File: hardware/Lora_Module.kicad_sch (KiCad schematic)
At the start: 9 parts, among them J2 85201239, U7 RFM95W-868S2

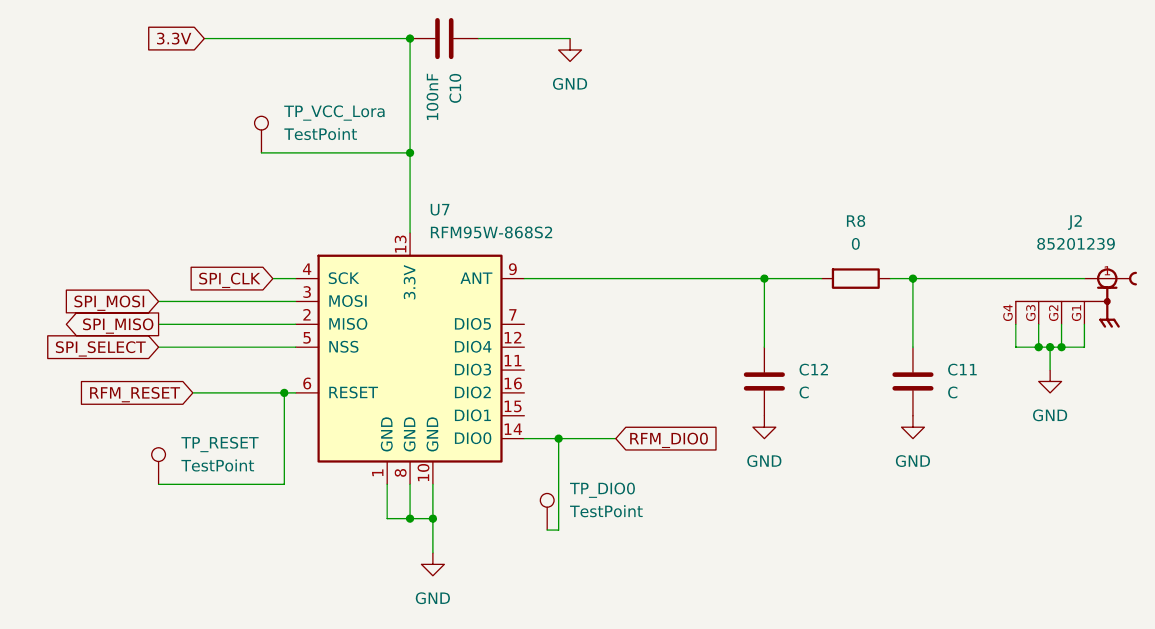
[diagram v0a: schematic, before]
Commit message: Ref composant JLCBPCB LoRa
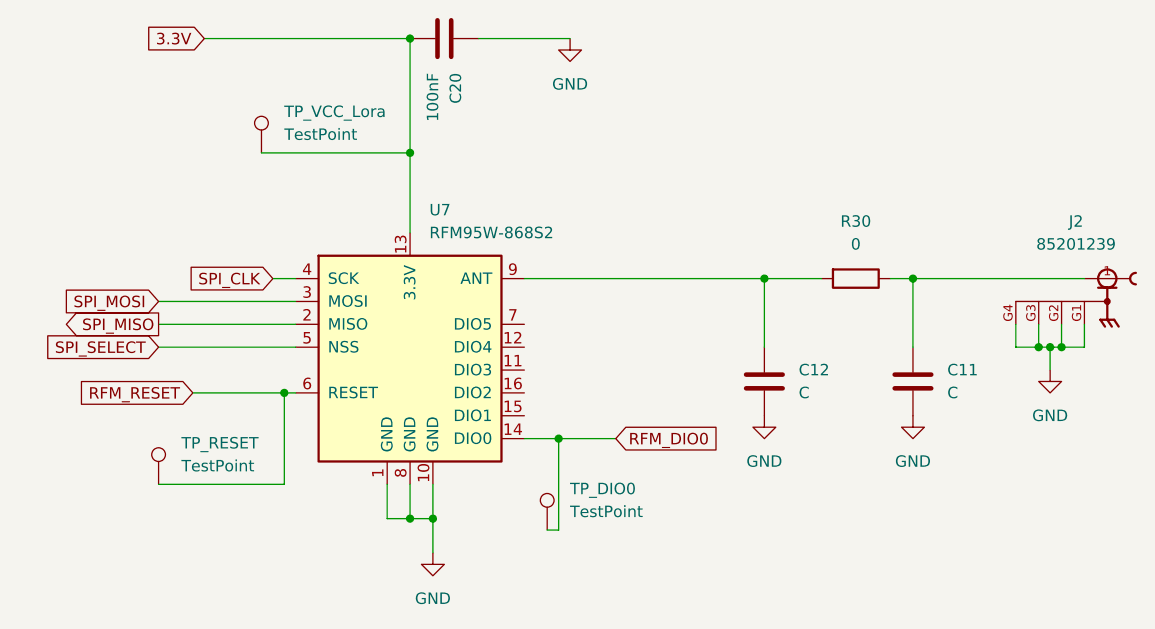
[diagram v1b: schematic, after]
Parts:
- C11, C12: footprint Capacitor_SMD:C_0805_2012Metric_Pad1.18x1.45mm_HandSolder -> Resistor_SMD:R_0805_2012Metric_Pad1.20x1.40mm_HandSolder; JLCPCB Part # (none) -> /; Package (none) -> 0805
- C20: renamed from C10; footprint Capacitor_SMD:C_0201_0603Metric -> Capacitor_SMD:C_0603_1608Metric; JLCPCB Part # (none) -> C1590; Package (none) -> 0603
- J2: JLCPCB Part # (none) -> C7498154; Package None -> Plugin
- R30: renamed from R8; JLCPCB Part # (none) -> /; Package (none) -> 0805
- U7: JLCPCB Part # (none) -> C2844472; Package (none) -> SMD,16x16mm
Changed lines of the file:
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@@
 			)
 		)
-		(property "Description" ""
+		(property "Description" "-45℃~+80℃ 1 14.6mm 4.65mm 50Ω 6GHz Board Side Inner Bore Plugin Coaxial Connectors (RF) ROHS"
 			(at 186.69 64.77 0)
 			(effects
@@
 			)
 		)
-		(property "Package" "None"
+		(property "Package" "Plugin"
 			(at 186.69 64.77 0)
 			(effects
@@
 				)
 				(justify bottom)
+				(hide yes)
+			)
+		)
+		(property "JLCPCB Part #" "C7498154"
+			(at 186.69 64.77 0)
+			(effects
+				(font
+					(size 1.27 1.27)
+				)
 				(hide yes)
 			)
@@
 			)
 		)
-		(property "Footprint" "Capacitor_SMD:C_0805_2012Metric_Pad1.18x1.45mm_HandSolder"
+		(property "Footprint" "Resistor_SMD:R_0805_2012Metric_Pad1.20x1.40mm_HandSolder"
 			(at 149.5552 80.01 0)
 			(effects
@@
 		)
 		(property "Description" "Unpolarized capacitor"
+			(at 148.59 76.2 0)
+			(effects
+				(font
+					(size 1.27 1.27)
+				)
+				(hide yes)
+			)
+		)
+		(property "JLCPCB Part #" "/"
+			(at 148.59 76.2 0)
+			(effects
+				(font
+					(size 1.27 1.27)
+				)
+				(hide yes)
+			)
+		)
+		(property "Package" "0805"
 			(at 148.59 76.2 0)
 			(effects
@@
 		(dnp no)
 		(fields_autoplaced yes)
-		(property "Reference" "R8"
+		(property "Reference" "R30"
 			(at 158.75 58.42 90)
 			(effects
@@
 			)
 		)
+		(property "Package" "0805"
+			(at 158.75 64.77 90)
+			(effects
+				(font
+					(size 1.27 1.27)
+				)
+				(hide yes)
+			)
+		)
+		(property "JLCPCB Part #" "/"
+			(at 158.75 64.77 90)
+			(effects
+				(font
+					(size 1.27 1.27)
+				)
+				(hide yes)
+			)
+		)
 		(pin "1"
 		)
@@
 			(project ""
 				(path "/5b969f6e-a36e-432b-8f00-b2d6a515a877/9db73a32-37a4-4249-8656-c1ba9b3afe01"
-					(reference "R8")
+					(reference "R30")
 					(unit 1)
 				)
@@
 			)
 		)
-		(property "Footprint" "Capacitor_SMD:C_0805_2012Metric_Pad1.18x1.45mm_HandSolder"
+		(property "Footprint" "Resistor_SMD:R_0805_2012Metric_Pad1.20x1.40mm_HandSolder"
 			(at 166.0652 80.01 0)
 			(effects
@@
 		)
 		(property "Description" "Unpolarized capacitor"
+			(at 165.1 76.2 0)
+			(effects
+				(font
+					(size 1.27 1.27)
+				)
+				(hide yes)
+			)
+		)
+		(property "JLCPCB Part #" "/"
+			(at 165.1 76.2 0)
+			(effects
+				(font
+					(size 1.27 1.27)
+				)
+				(hide yes)
+			)
+		)
+		(property "Package" "0805"
 			(at 165.1 76.2 0)
 			(effects
@@
 			)
 		)
+		(property "JLCPCB Part #" "C2844472"
+			(at 109.22 72.39 0)
+			(effects
+				(font
+					(size 1.27 1.27)
+				)
+				(hide yes)
+			)
+		)
+		(property "Package" "SMD,16x16mm"
+			(at 109.22 72.39 0)
+			(effects
+				(font
+					(size 1.27 1.27)
+				)
+				(hide yes)
+			)
+		)
 		(pin "3"
 		)
@@
 		(on_board yes)
 		(dnp no)
-		(property "Reference" "C10"
+		(property "Reference" "C20"
 			(at 114.3001 41.91 0)
 			(effects
@@
 			)
 		)
-		(property "Footprint" "Capacitor_SMD:C_0201_0603Metric"
+		(property "Footprint" "Capacitor_SMD:C_0603_1608Metric"
 			(at 109.22 39.0652 0)
 			(effects
@@
 			)
 		)
-		(property "Description" "Unpolarized capacitor"
+		(property "Description" "100nF 25V X7R ±10% 0603 Multilayer Ceramic Capacitors MLCC - SMD/SMT ROHS"
 			(at 113.03 38.1 0)
 			(effects
@@
 			)
 		)
+		(property "JLCPCB Part #" "C1590"
+			(at 113.03 38.1 0)
+			(effects
+				(font
+					(size 1.27 1.27)
+				)
+				(hide yes)
+			)
+		)
+		(property "Package" "0603"
+			(at 113.03 38.1 0)
+			(effects
+				(font
+					(size 1.27 1.27)
+				)
+				(hide yes)
+			)
+		)
 		(pin "2"
 		)
@@
 			(project "GOG"
 				(path "/5b969f6e-a36e-432b-8f00-b2d6a515a877/9db73a32-37a4-4249-8656-c1ba9b3afe01"
-					(reference "C10")
-					(unit 1)
-				)
+					(reference "C20")
+					(unit 1)
+				)

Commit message: Fix schematic components annotations
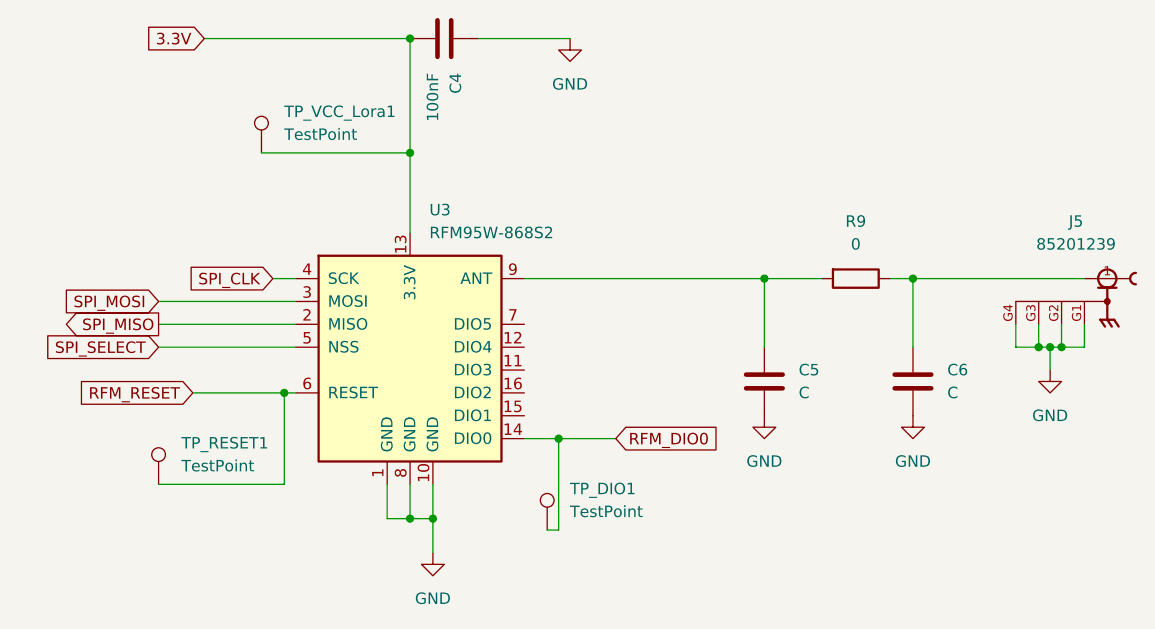
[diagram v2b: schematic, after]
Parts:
- renumbered C20 to C4, C12 to C5, C11 to C6, J2 to J5, R30 to R9, TP_DIO0 to TP_DIO1, TP_RESET to TP_RESET1, TP_VCC_Lora to TP_VCC_Lora1, U7 to U3
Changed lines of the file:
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@@
 		(dnp no)
 		(fields_autoplaced yes)
-		(property "Reference" "TP_DIO0"
+		(property "Reference" "TP_DIO1"
 			(at 127 88.1379 0)
 			(effects
@@
 			(project ""
 				(path "/5b969f6e-a36e-432b-8f00-b2d6a515a877/9db73a32-37a4-4249-8656-c1ba9b3afe01"
-					(reference "TP_DIO0")
+					(reference "TP_DIO1")
 					(unit 1)
 				)
@@
 		(on_board yes)
 		(dnp no)
-		(property "Reference" "J2"
+		(property "Reference" "J5"
 			(at 183.2229 58.42 0)
 			(effects
@@
 			(project ""
 				(path "/5b969f6e-a36e-432b-8f00-b2d6a515a877/9db73a32-37a4-4249-8656-c1ba9b3afe01"
-					(reference "J2")
+					(reference "J5")
 					(unit 1)
 				)
@@
 		(dnp no)
 		(fields_autoplaced yes)
-		(property "Reference" "C12"
+		(property "Reference" "C5"
 			(at 152.4 74.9299 0)
 			(effects
@@
 			(project ""
 				(path "/5b969f6e-a36e-432b-8f00-b2d6a515a877/9db73a32-37a4-4249-8656-c1ba9b3afe01"
-					(reference "C12")
+					(reference "C5")
 					(unit 1)
 				)
@@
 		(dnp no)
 		(fields_autoplaced yes)
-		(property "Reference" "R30"
+		(property "Reference" "R9"
 			(at 158.75 58.42 90)
 			(effects
@@
 			(project ""
 				(path "/5b969f6e-a36e-432b-8f00-b2d6a515a877/9db73a32-37a4-4249-8656-c1ba9b3afe01"
-					(reference "R30")
+					(reference "R9")
 					(unit 1)
 				)
@@
 		(dnp no)
 		(fields_autoplaced yes)
-		(property "Reference" "TP_RESET"
+		(property "Reference" "TP_RESET1"
 			(at 83.82 83.0579 0)
 			(effects
@@
 			(project ""
 				(path "/5b969f6e-a36e-432b-8f00-b2d6a515a877/9db73a32-37a4-4249-8656-c1ba9b3afe01"
-					(reference "TP_RESET")
+					(reference "TP_RESET1")
 					(unit 1)
 				)
@@
 		(dnp no)
 		(fields_autoplaced yes)
-		(property "Reference" "C11"
+		(property "Reference" "C6"
 			(at 168.91 74.9299 0)
 			(effects
@@
 			(project ""
 				(path "/5b969f6e-a36e-432b-8f00-b2d6a515a877/9db73a32-37a4-4249-8656-c1ba9b3afe01"
-					(reference "C11")
+					(reference "C6")
 					(unit 1)
 				)
@@
 		(dnp no)
 		(fields_autoplaced yes)
-		(property "Reference" "U7"
+		(property "Reference" "U3"
 			(at 111.3633 57.15 0)
 			(effects
@@
 			(project ""
 				(path "/5b969f6e-a36e-432b-8f00-b2d6a515a877/9db73a32-37a4-4249-8656-c1ba9b3afe01"
-					(reference "U7")
+					(reference "U3")
 					(unit 1)
 				)
@@
 		(dnp no)
 		(fields_autoplaced yes)
-		(property "Reference" "#PWR06"
+		(property "Reference" "#PWR011"
 			(at 127 44.45 0)
 			(effects
@@
 			(project ""
 				(path "/5b969f6e-a36e-432b-8f00-b2d6a515a877/9db73a32-37a4-4249-8656-c1ba9b3afe01"
-					(reference "#PWR06")
+					(reference "#PWR011")
 					(unit 1)
 				)
@@
 		(dnp no)
 		(fields_autoplaced yes)
-		(property "Reference" "TP_VCC_Lora"
+		(property "Reference" "TP_VCC_Lora1"
 			(at 95.25 46.2279 0)
 			(effects
@@
 			(project ""
 				(path "/5b969f6e-a36e-432b-8f00-b2d6a515a877/9db73a32-37a4-4249-8656-c1ba9b3afe01"
-					(reference "TP_VCC_Lora")
+					(reference "TP_VCC_Lora1")
 					(unit 1)
 				)
@@
 		(dnp no)
 		(fields_autoplaced yes)
-		(property "Reference" "#PWR017"
+		(property "Reference" "#PWR014"
 			(at 165.1 86.36 0)
 			(effects
@@
 			(project ""
 				(path "/5b969f6e-a36e-432b-8f00-b2d6a515a877/9db73a32-37a4-4249-8656-c1ba9b3afe01"
-					(reference "#PWR017")
+					(reference "#PWR014")
 					(unit 1)
 				)
@@
 		(dnp no)
 		(fields_autoplaced yes)
-		(property "Reference" "#PWR018"
+		(property "Reference" "#PWR013"
 			(at 148.59 86.36 0)
 			(effects
@@
 			(project ""
 				(path "/5b969f6e-a36e-432b-8f00-b2d6a515a877/9db73a32-37a4-4249-8656-c1ba9b3afe01"
-					(reference "#PWR018")
+					(reference "#PWR013")
 					(unit 1)
 				)
@@
 		(on_board yes)
 		(dnp no)
-		(property "Reference" "C20"
+		(property "Reference" "C4"
 			(at 114.3001 41.91 0)
 			(effects
@@
 			(project "GOG"
 				(path "/5b969f6e-a36e-432b-8f00-b2d6a515a877/9db73a32-37a4-4249-8656-c1ba9b3afe01"
-					(reference "C20")
+					(reference "C4")
 					(unit 1)
 				)
@@
 		(dnp no)
 		(fields_autoplaced yes)
-		(property "Reference" "#PWR07"
+		(property "Reference" "#PWR015"
 			(at 111.76 101.6 0)
 			(effects
@@
 			(project ""
 				(path "/5b969f6e-a36e-432b-8f00-b2d6a515a877/9db73a32-37a4-4249-8656-c1ba9b3afe01"
-					(reference "#PWR07")
+					(reference "#PWR015")
 					(unit 1)
 				)
@@
 		(dnp no)
 		(fields_autoplaced yes)
-		(property "Reference" "#PWR09"
+		(property "Reference" "#PWR012"
 			(at 180.34 81.28 0)
 			(effects
@@
 			(project ""
 				(path "/5b969f6e-a36e-432b-8f00-b2d6a515a877/9db73a32-37a4-4249-8656-c1ba9b3afe01"
-					(reference "#PWR09")
-					(unit 1)
-				)
+					(reference "#PWR012")
+					(unit 1)
+				)
